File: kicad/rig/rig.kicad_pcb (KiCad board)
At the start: 4 copper layers, 160 x 100 mm, 48 parts, among them J1 Baud rate set, J2 TTL-USB, J3 5V DC, SW1 RESET, SW2 POWER, U1 DCJ11, U2 DC319, U3 SN74AHCT14N, U4 74F821SPC, U5 74AHCT541, U6 GAL20V8A-15LP, Y1 4000 kHz, Y2 614.4 kHz

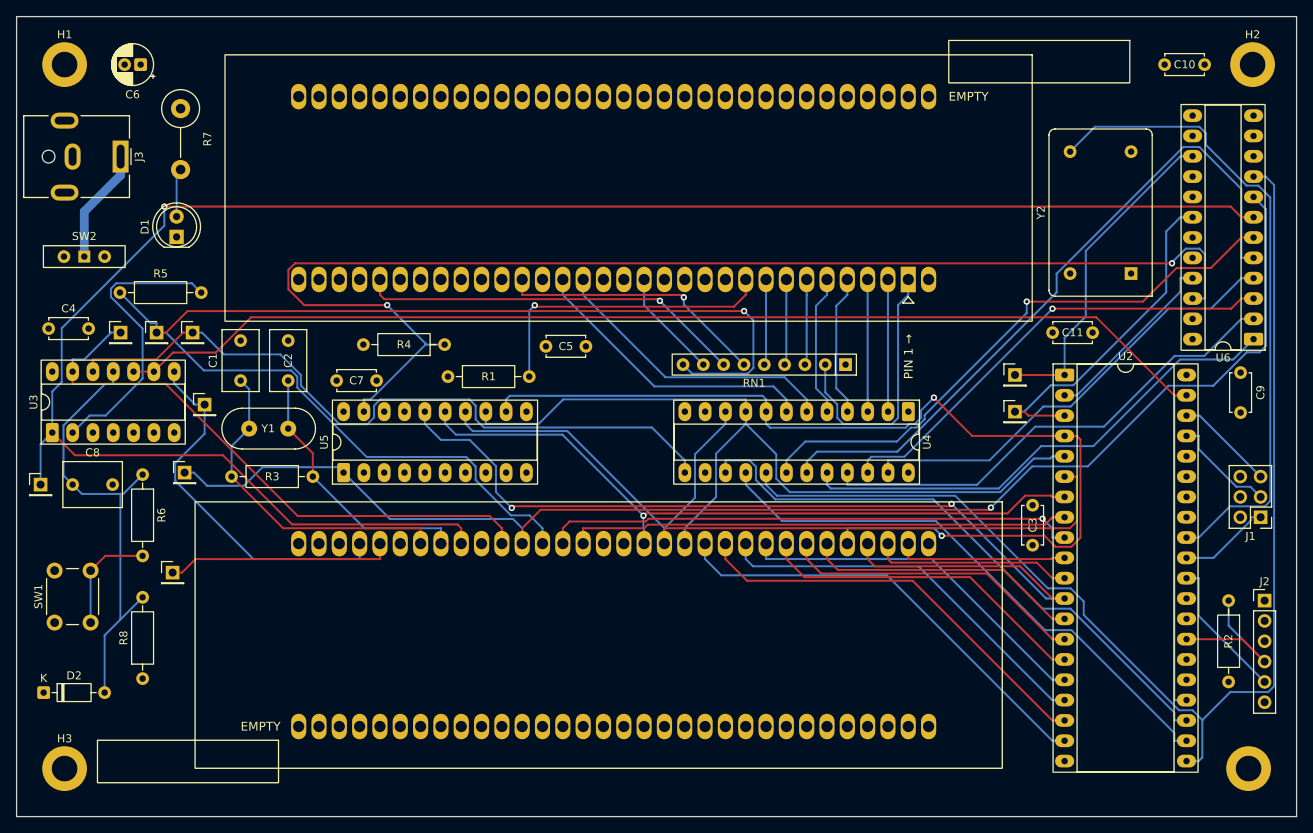
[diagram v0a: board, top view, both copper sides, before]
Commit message: Widen ZIF pads and clear GPREAD routing around socket end
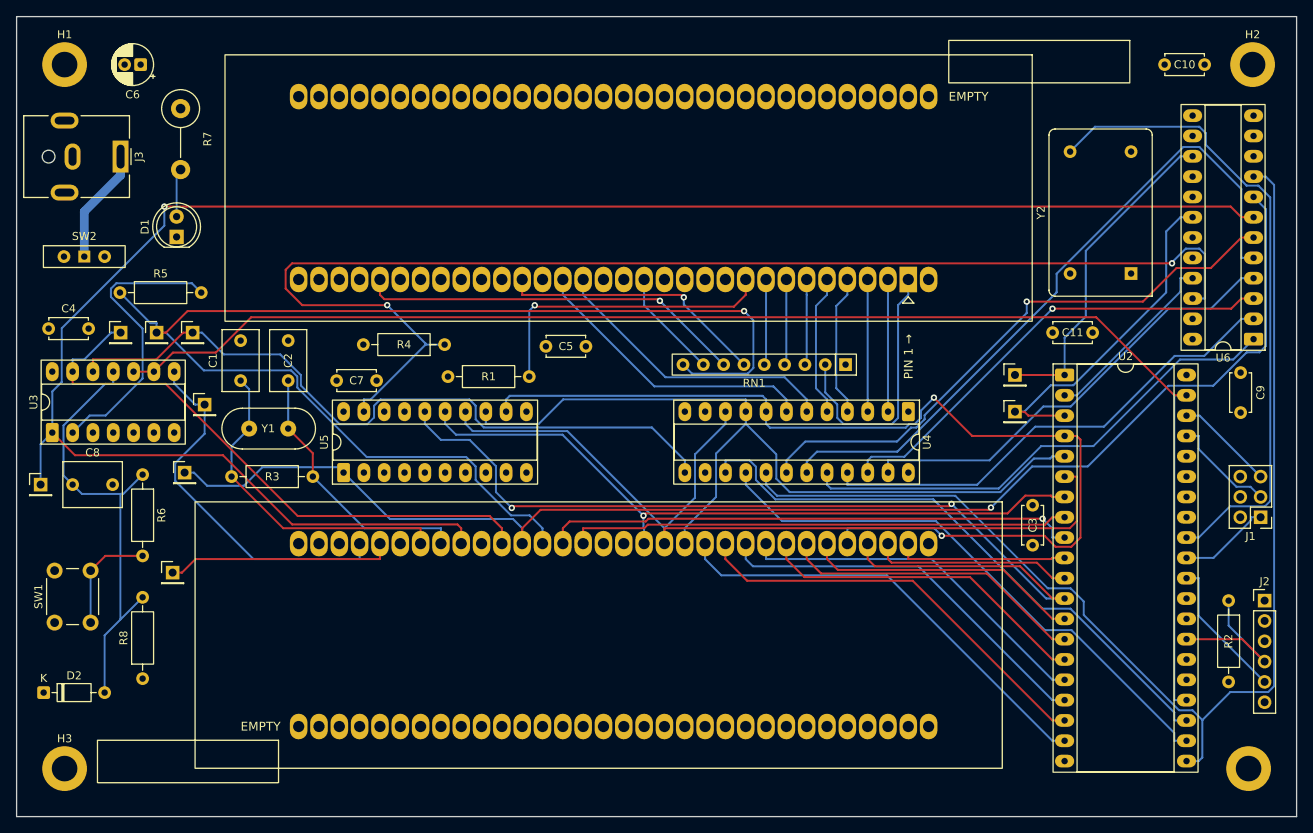
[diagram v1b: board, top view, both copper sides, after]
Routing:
- net /~{GPREAD}: track 160.1 -> 160.7 mm
